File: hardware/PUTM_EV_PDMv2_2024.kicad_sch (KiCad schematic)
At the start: 13 parts, among them J6 FTSH-107-01-L-DV-K-A, J7 USB_C_Receptacle_USB2.0_14P, U1 STM32G0C1KCTxN

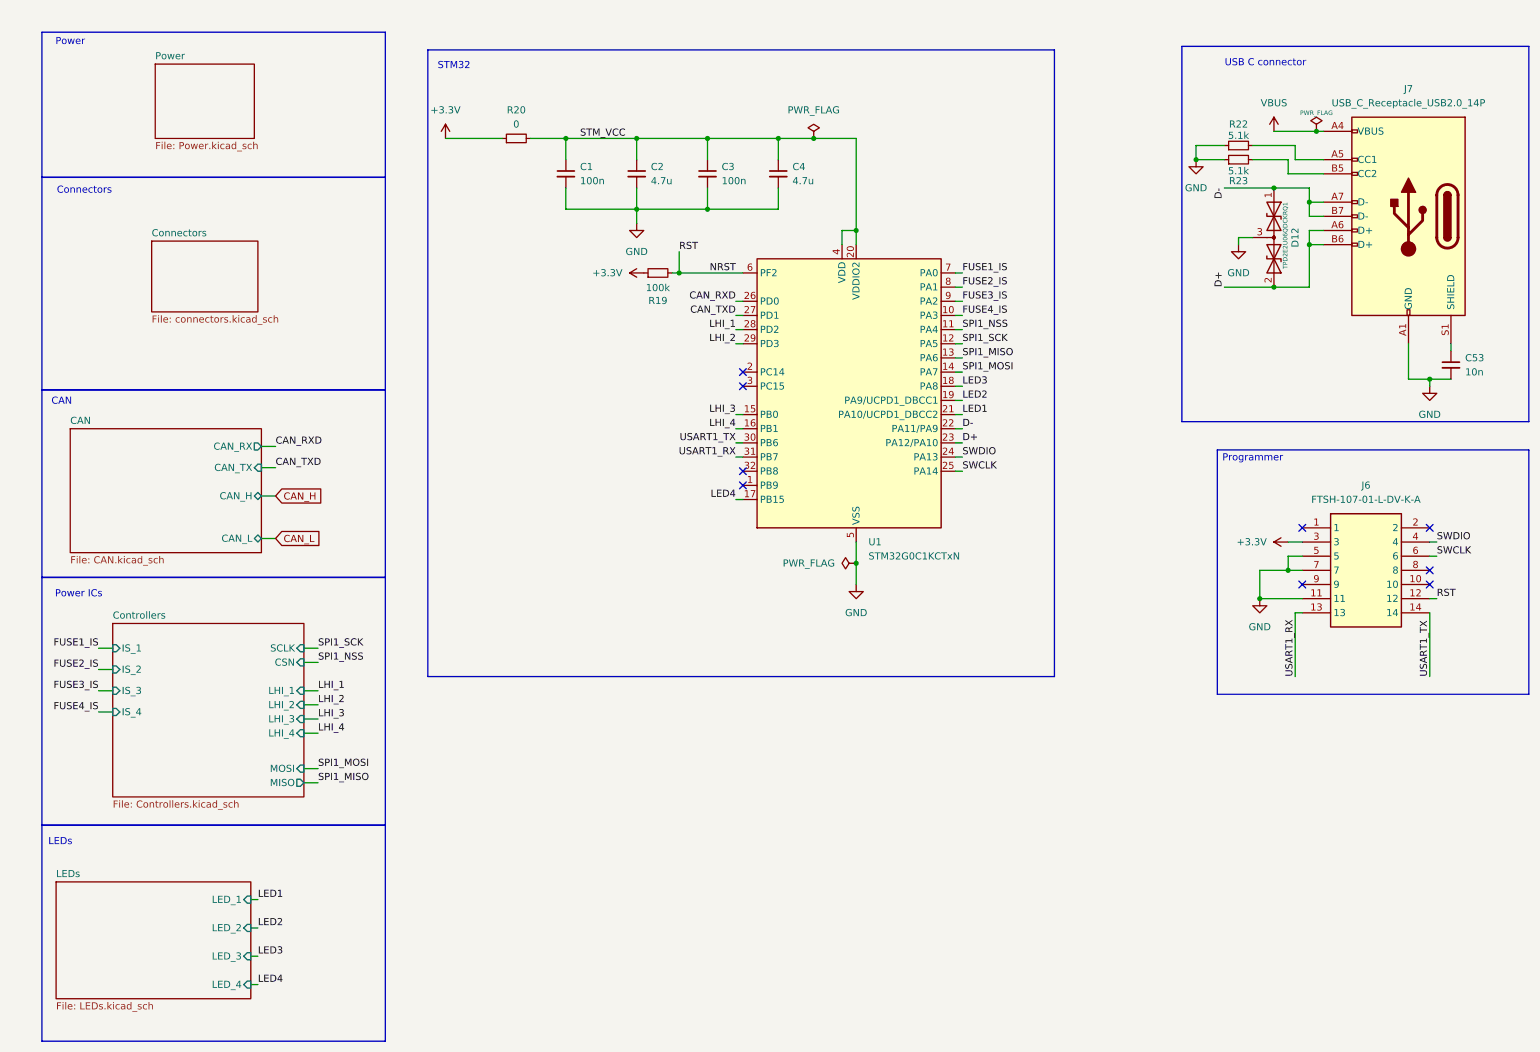
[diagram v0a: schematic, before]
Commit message: cube->cmake port, current calc fix, spi datalength fix, hard-v1.1.0 sync
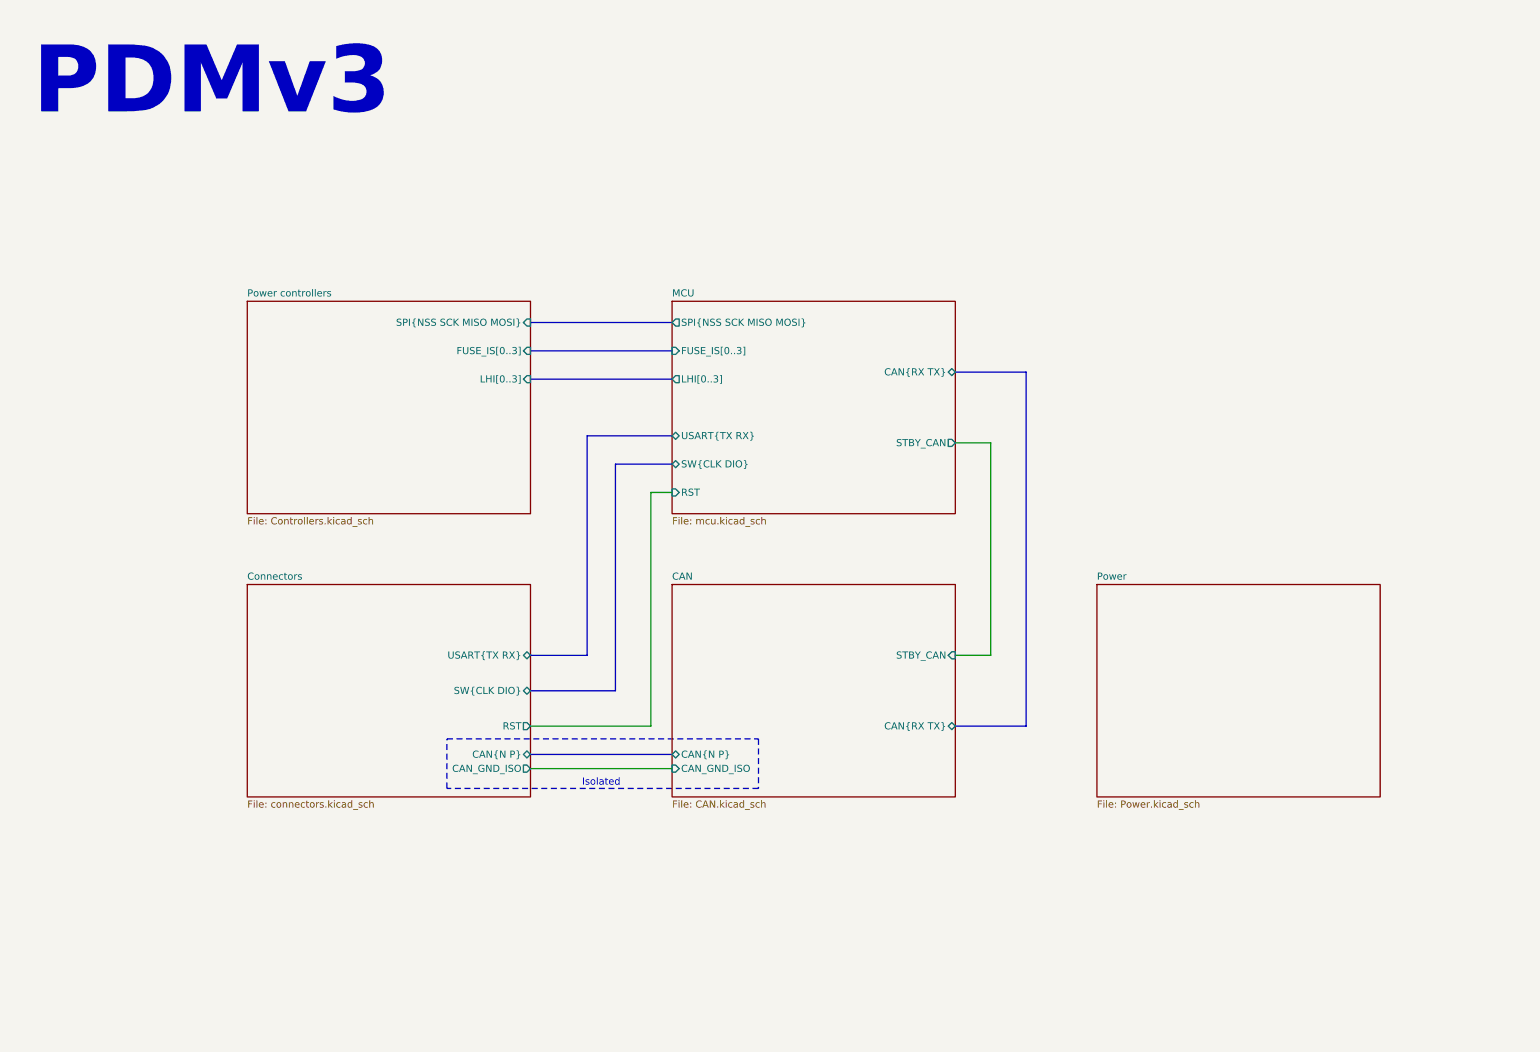
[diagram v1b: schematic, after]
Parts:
- removed C1, C3: 100n, Capacitor_SMD:C_0603_1608Metric, symbol Device:C_Small
- removed C2, C4: 4.7u, Capacitor_SMD:C_0603_1608Metric, symbol Device:C_Small
- removed C53: 10n, Capacitor_SMD:C_0603_1608Metric_Pad1.08x0.95mm_HandSolder, symbol Device:C_Small
- removed D12: TPD2E2U06QDCKRQ1, Package_TO_SOT_SMD:SOT-323_SC-70_Handsoldering, symbol Device:D_TVS_Dual_AAC
- removed J6: FTSH-107-01-L-DV-K-A, FTSH-107-XX-YYY-DV-K-A, symbol FTSH-107-01-L-DV-K-A:FTSH-107-01-L-DV-K-A
- removed J7: USB_C_Receptacle_USB2.0_14P, Connector_USB:USB_C_Receptacle_JAE_DX07S024WJ3R400, symbol usb_c_receptacle_usb2.0_14p:USB_C_Receptacle_USB2.0_14P
- removed R19: 100k, Resistor_SMD:R_0603_1608Metric, symbol Device:R_Small
- removed R20: 0, Resistor_SMD:R_0603_1608Metric_Pad0.98x0.95mm_HandSolder, symbol Device:R_Small
- removed R22, R23: 5.1k, Resistor_SMD:R_0603_1608Metric_Pad0.98x0.95mm_HandSolder, symbol Device:R_Small
- removed U1: STM32G0C1KCTxN, Package_QFP:LQFP-32_7x7mm_P0.8mm, symbol MCU_ST_STM32G0:STM32G0C1KCTxN
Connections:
- no-connect marks 9 -> 0
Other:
- sheet Controllers renamed Power controllers
- removed sheet LEDs
- added sheet MCU (mcu.kicad_sch)
- sheet CAN ports: added CAN_GND_ISO, CAN{N P}, CAN{RX TX}, STBY_CAN; removed CAN_H, CAN_L, CAN_RX, CAN_TX
- sheet Connectors ports: added CAN_GND_ISO, CAN{N P}, RST, SW{CLK DIO}, USART{TX RX}; removed none
- sheet Power controllers ports: added FUSE_IS[0..3], LHI[0..3], SPI{NSS SCK MISO MOSI}; removed CSN, IS_1, IS_2, IS_3, IS_4, LHI_1, LHI_2, LHI_3, LHI_4, MISO, MOSI, SCLK
- note added: "Isolated"
- note added: "PDMv3"
- note removed: "CAN"
- note removed: "Connectors"
- note removed: "LEDs"
- note removed: "Power"
- note removed: "Power ICs"
- note removed: "Programmer"
- note removed: "STM32"
- note removed: "USB C connector"
- company: Author: -> Authors: Grzegorz Potocki Jędrzej Kasprzyk
- title: (none) -> PDUv3
